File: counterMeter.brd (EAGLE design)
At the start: 100 x 64.4 mm, 128 parts, among them IC1 74AC14D, IC2 REG1117, IC3 74AC74D, IC4 74HC151D, IC5 74AC390D, IC6 74HC595D, IC7 74HC595D, J1 COMMON, J2 U/I/R, J3 10A, J4 U/I/R, K1 G6K-2P-Y, K2 G6K-2P-Y, K3 G6K-2P-Y, K4 G6K-2P-Y, K5 G6K-2P-Y, T1 BC847, T10 BC847, T2 BC847, T3 BC847, T4 BC847, T5 BC857, T6 BC857, T7 BC857, T8 BC857, T9 BC857, U1 MAX9201, U2 74XX161, U3 SN74LVC2G157DCTR, U4 MAX871, U5 AD8638, U6 AD8539

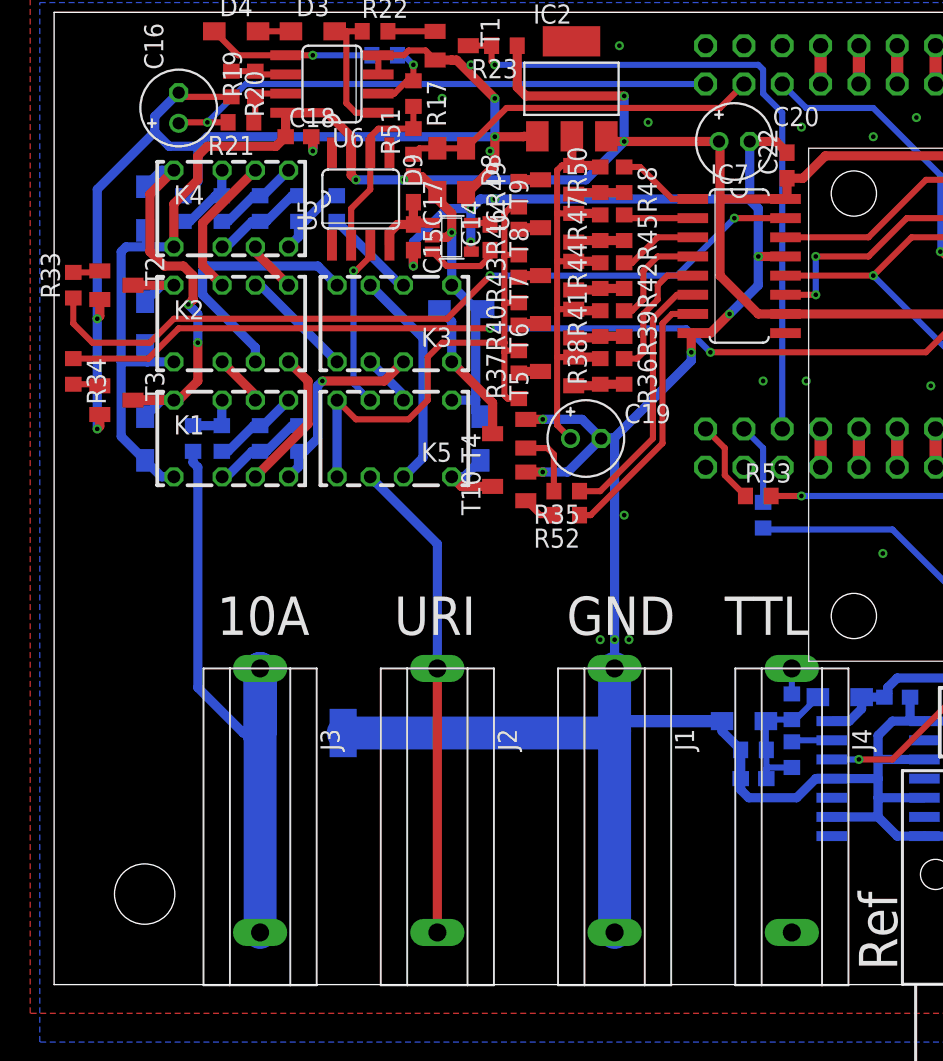
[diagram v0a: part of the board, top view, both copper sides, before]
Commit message: some input protection + buffer output filter
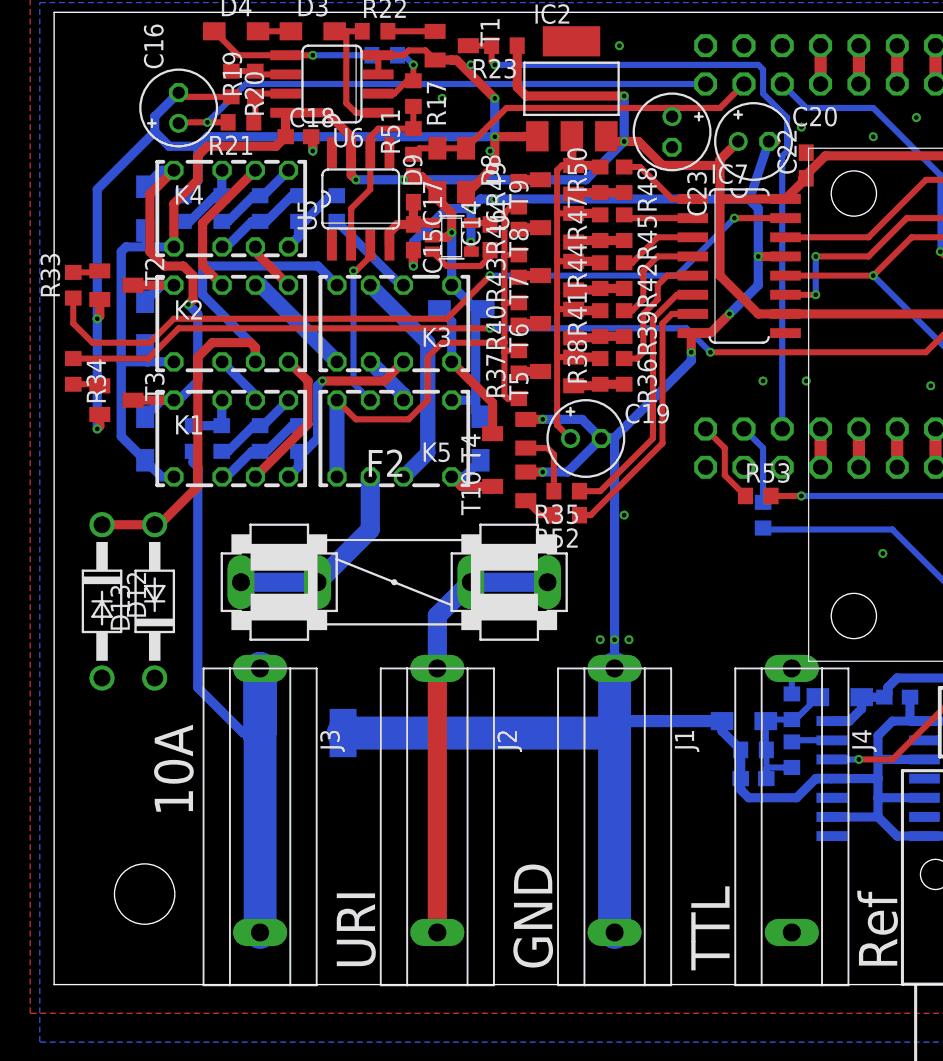
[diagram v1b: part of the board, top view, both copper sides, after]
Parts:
- added C23: 10µ, rcl:E2-5
- added D12, D13: 1N4001, diode:DO41-10
- added F2: (no value), special:FUSE1
- moved C20 1.27 mm to (46.4, 55.9)
- moved C22 1.27 mm to (49.8, 54.3)
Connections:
- new net N$19: F2.1A, F2.1B, K5.6
- net GND: now also C23.-, D12.A, D13.C
- net I_IN: now also D12.C, D13.A
- net I_U/I/R: now also F2.2A, F2.2B; no longer K5.6
- net PA1: now also C23.+
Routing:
- net I_IN: track 17.0 -> 38.3 mm
- net N$19: track 0.00 -> 13.5 mm
- net I_U/I/R: track 32.0 -> 29.2 mm
- net N$45: track 29.2 -> 26.5 mm, vias 2 -> 1
- net GND: track 492.4 -> 490.3 mm, vias 75 -> 74
- net VCC: track 343.0 -> 343.9 mm
- net PA1: track 23.8 -> 24.4 mm

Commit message: more minor pcb changes
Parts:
- F2: value (none) -> 315mA
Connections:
- net N$9: now also J4.1@2
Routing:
- net N$9: track 1.69 -> 19.2 mm
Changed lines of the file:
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@@
 <element name="D12" library="diode" package="DO41-10" value="1N4001" x="3.175" y="25.4" rot="R270"/>
 <element name="D13" library="diode" package="DO41-10" value="1N4001" x="6.6675" y="25.4" rot="R90"/>
-<element name="F2" library="special" package="FUSE1" value="" x="22.5425" y="26.67"/>
+<element name="F2" library="special" package="FUSE1" value="315mA" x="22.5425" y="26.67"/>
 <element name="C23" library="rcl" package="E2-5" value="10µ" x="40.9575" y="56.515" rot="R270"/>
 </elements>
@@
 <contactref element="J4" pad="1@1"/>
 <wire x1="48.895" y1="20.955" x2="48.895" y2="19.265" width="0.4064" layer="16"/>
+<contactref element="J4" pad="1@2"/>
+<wire x1="48.895" y1="3.455" x2="48.895" y2="20.955" width="0.4064" layer="1"/>
 </signal>
 <signal name="N$10">
